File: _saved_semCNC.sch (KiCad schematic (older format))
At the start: 42 parts, among them P19 POWER_HEAD, P2 LPT port, P4 EXPANDER PAD, P5 CONN_01X02, P6 CONN_01X02, T1 TRANSFO, U1 MSP430G2452, U2 TIdac08s085, U3 LD1117S33CTR, U4 SPX2920U-3.3

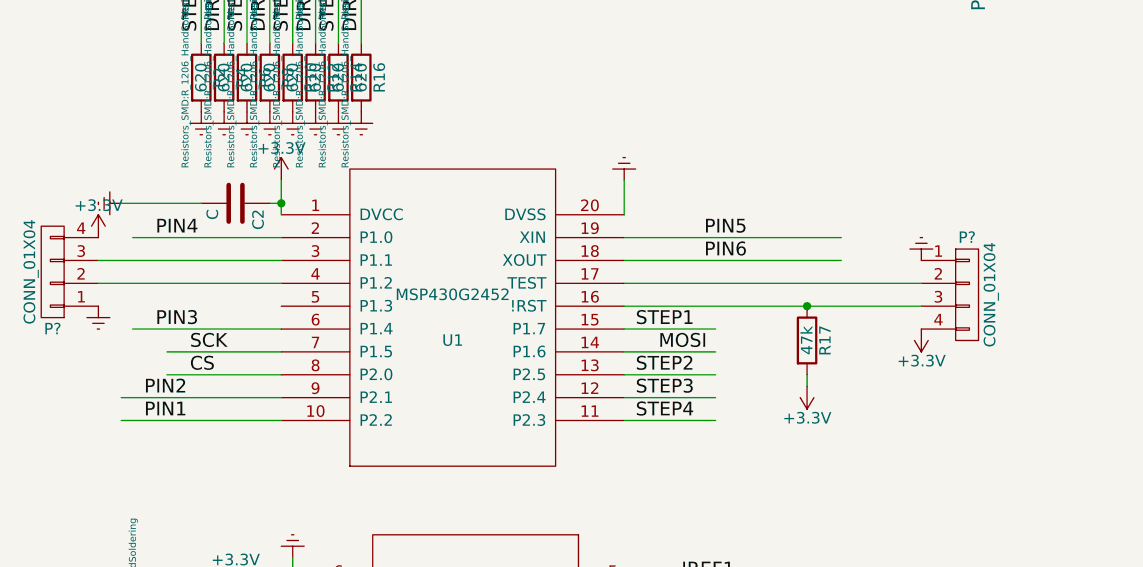
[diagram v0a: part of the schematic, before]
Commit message: trafo bent
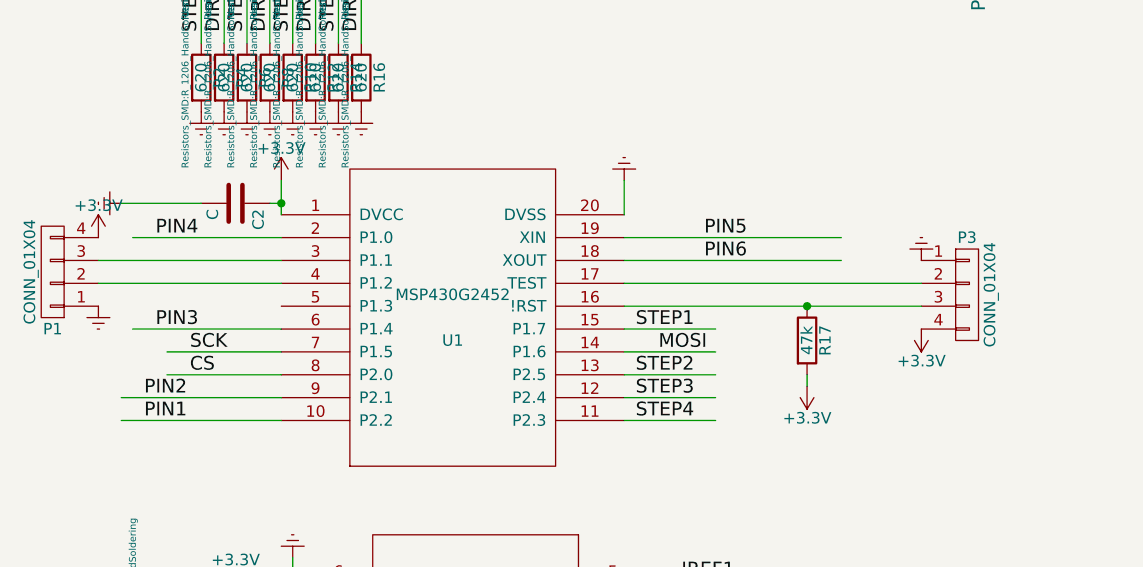
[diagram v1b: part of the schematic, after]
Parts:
- P1, P3: renamed from P?; footprint (none) -> Pin_Headers:Pin_Header_Straight_1x04
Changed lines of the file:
@@
 VMOT_GND
 $Comp
-L CONN_01X04 P?
+L CONN_01X04 P3
 U 1 1 561A45B9
 P 4600 2950
-F 0 "P?" H 4600 3200 50  0000 C CNN
+F 0 "P3" H 4600 3200 50  0000 C CNN
 F 1 "CONN_01X04" V 4700 2950 50  0000 C CNN
-F 2 "" H 4600 2950 60  0000 C CNN
+F 2 "Pin_Headers:Pin_Header_Straight_1x04" H 4600 2950 60  0001 C CNN
 F 3 "" H 4600 2950 60  0000 C CNN
 	1    4600 2950
@@
 $EndComp
 $Comp
-L +3.3V #PWR?
+L +3.3V #PWR032
 U 1 1 561A4FC2
 P 4400 3100
-F 0 "#PWR?" H 4400 2950 50  0001 C CNN
+F 0 "#PWR032" H 4400 2950 50  0001 C CNN
 F 1 "+3.3V" H 4400 3240 50  0000 C CNN
 F 2 "" H 4400 3100 60  0000 C CNN
@@
 $EndComp
 $Comp
-L Earth #PWR?
+L Earth #PWR033
 U 1 1 561A581B
 P 4400 2800
-F 0 "#PWR?" H 4400 2550 50  0001 C CNN
+F 0 "#PWR033" H 4400 2550 50  0001 C CNN
 F 1 "Earth" H 4400 2650 50  0001 C CNN
 F 2 "" H 4400 2800 60  0000 C CNN
@@
 $EndComp
 $Comp
-L CONN_01X04 P?
+L CONN_01X04 P1
 U 1 1 561A722D
 P 600 2850
-F 0 "P?" H 600 3100 50  0000 C CNN
+F 0 "P1" H 600 3100 50  0000 C CNN
 F 1 "CONN_01X04" V 700 2850 50  0000 C CNN
-F 2 "" H 600 2850 60  0000 C CNN
+F 2 "Pin_Headers:Pin_Header_Straight_1x04" H 600 2850 60  0001 C CNN
 F 3 "" H 600 2850 60  0000 C CNN
 	1    600  2850
@@
 $EndComp
 $Comp
-L Earth #PWR?
+L Earth #PWR034
 U 1 1 561A7FF5
 P 800 3000
-F 0 "#PWR?" H 800 2750 50  0001 C CNN
+F 0 "#PWR034" H 800 2750 50  0001 C CNN
 F 1 "Earth" H 800 2850 50  0001 C CNN
 F 2 "" H 800 3000 60  0000 C CNN
